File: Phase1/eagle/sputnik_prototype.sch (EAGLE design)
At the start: 83 parts, among them U1 MEGA128-M, U2 MIC5219 3.3V, Y1 32MHz, Y2 8MHZ

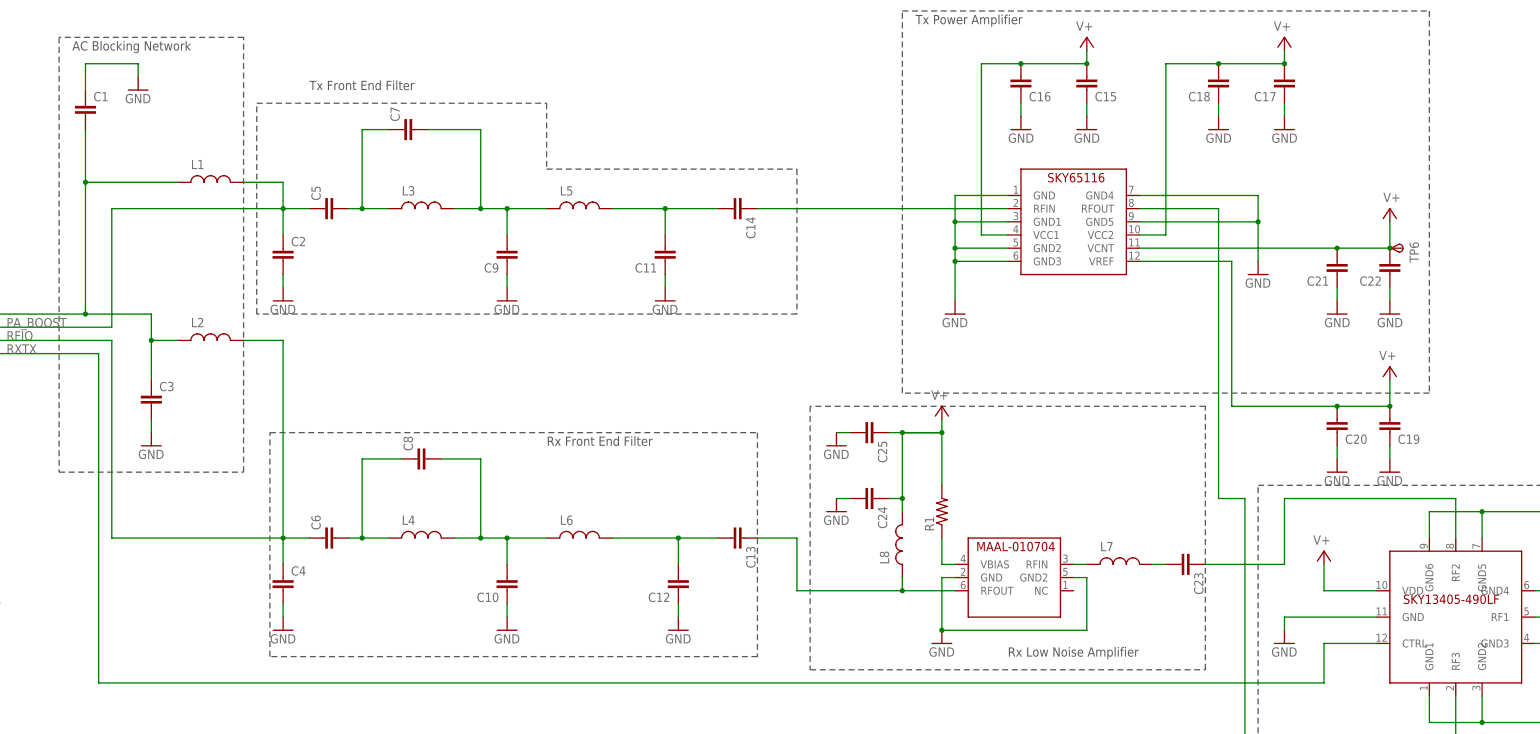
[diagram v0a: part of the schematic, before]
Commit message: Updated RF schematic
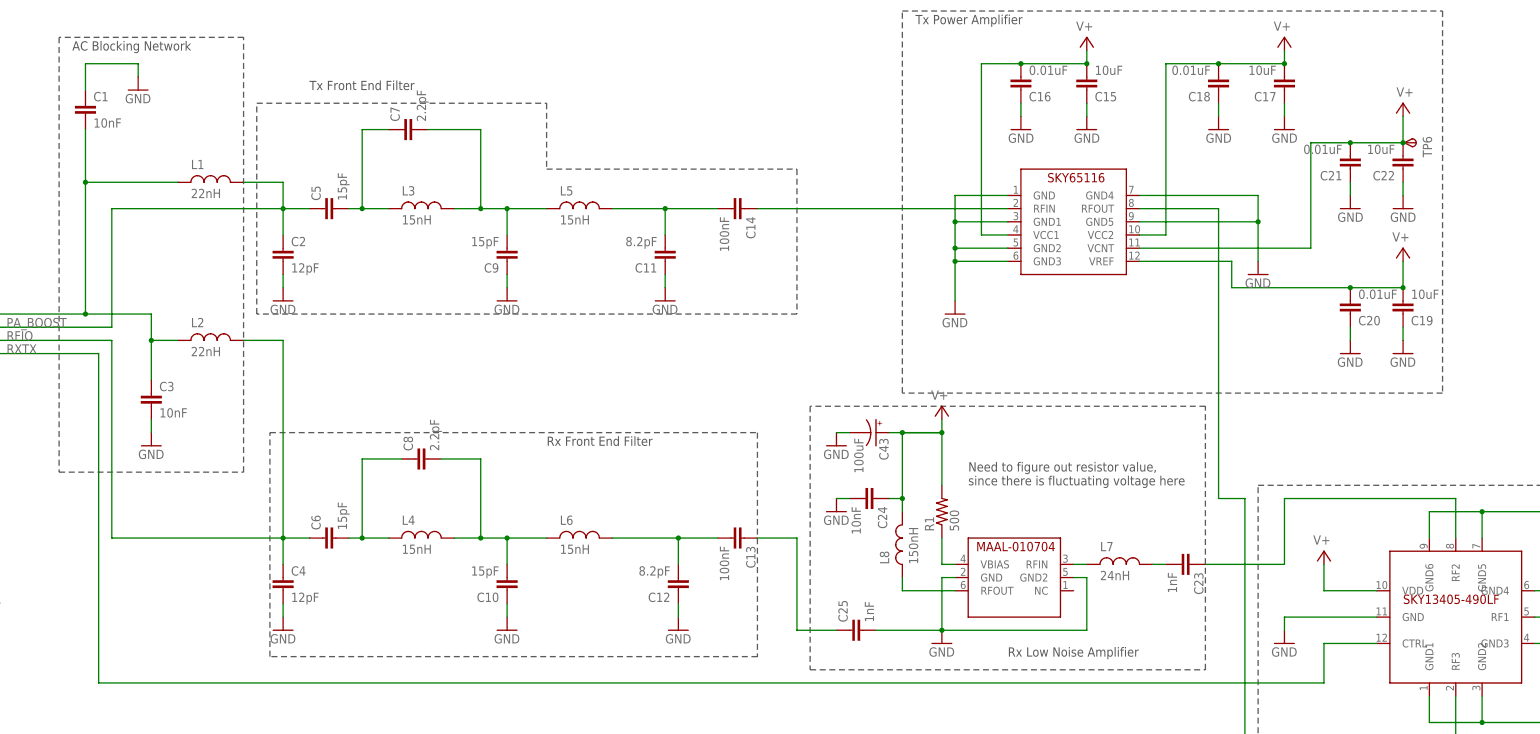
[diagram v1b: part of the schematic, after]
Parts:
- added C43: 100uF, rcl:CPOL-USCT6032
- C1, C3: value (none) -> 10nF
- C10, C5, C6, C9: value (none) -> 15pF
- C11, C12: value (none) -> 8.2pF
- C13, C14: value (none) -> 100nF
- C15, C17, C19, C22: value (none) -> 10uF
- C16, C18, C20, C21: value (none) -> 0.01uF
- C2, C4: value (none) -> 12pF
- C23, C25: value (none) -> 1nF; device rcl_custom:C-EU0603-B-NOSILK -> rcl_custom:C-EU0402-B-NOSILK
- C24: value (none) -> 10nF; device rcl_custom:C-EU0603-B-NOSILK -> rcl_custom:C-EU0402-B-NOSILK
- C7, C8: value (none) -> 2.2pF
- L1, L2: value (none) -> 22nH
- L3, L4, L5, L6: value (none) -> 15nH
- L7: value (none) -> 24nH; device rcl_custom:L-US0603-B-NOSILK -> rcl_custom:L-US0402-B-NOSILK
- L8: value (none) -> 150nH
- R1: value (none) -> 500
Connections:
- new net N$7: L8.1, U$4.RFOUT
- net GND: now also C43.-
- net N$4: now also C25.1; no longer L8.1, U$4.RFOUT
- net V+: now also C43.+; no longer C25.1
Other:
- note added: "Need to figure out resistor value, since there is fluctuating voltage here"
- moved on the sheet: C19, C20, C21, C22, C25, TP6

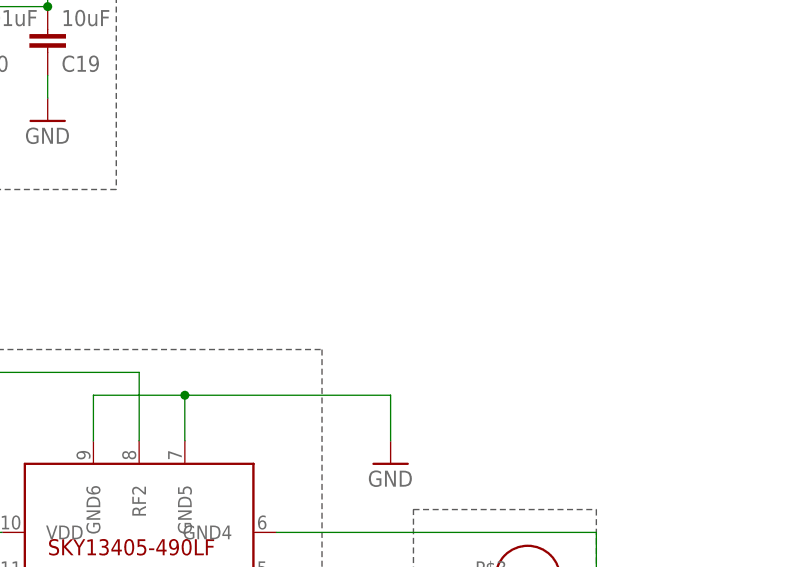
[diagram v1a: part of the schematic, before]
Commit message: Updated RF schematic
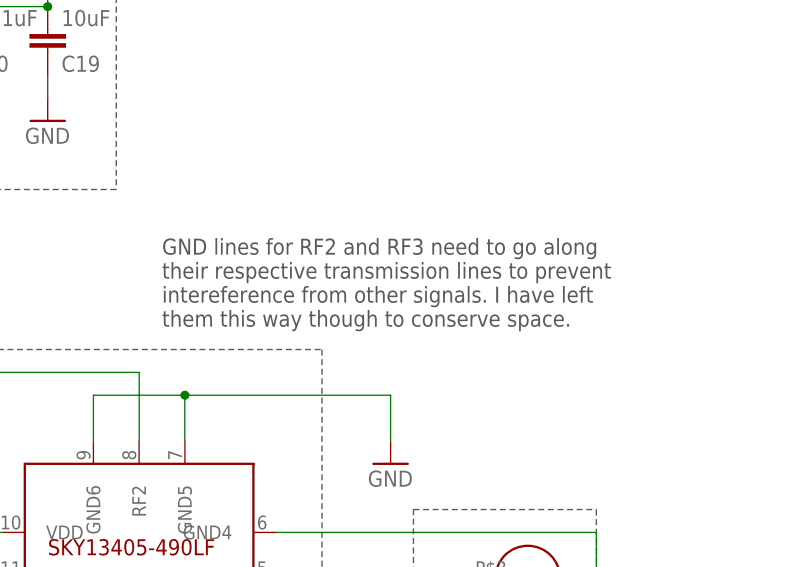
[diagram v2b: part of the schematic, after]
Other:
- note added: "GND lines for RF2 and RF3 need to go along their respective transmission lines to prevent intereference from other signals. I have left them this way though to conserve space."
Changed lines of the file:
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@@
 <?xml version="1.0" encoding="utf-8"?>
 <!DOCTYPE eagle SYSTEM "eagle.dtd">
-<eagle version="7.5.0">
+<eagle version="7.4.0">
 <drawing>
 <settings>
@@
 <text x="406.4" y="332.74" size="1.778" layer="97">Need to figure out resistor value,
 since there is fluctuating voltage here</text>
+<text x="502.92" y="335.28" size="1.778" layer="97">GND lines for RF2 and RF3 need to go along
+their respective transmission lines to prevent
+intereference from other signals. I have left
+them this way though to conserve space.</text>
 </plain>
 <instances>

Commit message: Updated the schematic a bit. Removed I2C line to payload and sense pin
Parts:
- removed JP6: (no value), psas_c3_team05:PINHD-1X2
- removed JP7: (no value), pinhead:PINHD-1X3
- removed TP2, TP3, TP6, TP7, TP8, TP9: TPSPAD1-13, testpad:TPSPAD1-13
- C23: value 1nF -> (none)
- C24: value 10nF -> (none)
- C43: value 100uF -> (none)
- L7: value 24nH -> (none)
- L8: value 150nH -> (none)
- R1: value 500 -> (none)
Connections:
- net PE4: no longer JP7.1, TP7.PP
- net PE5: no longer JP7.2, TP8.PP
- net PE6: no longer JP7.3, TP9.PP
- net SDA: no longer JP6.2, TP3.PP
- net SDL: no longer JP6.1, TP2.PP
- net V+: no longer TP6.PP
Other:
- note added: "Need to figure out values for LNA"
- note removed: "Need to figure out resistor value, since there is fluctuating voltage here"
- note removed: "Sense"
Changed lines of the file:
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@@
 <part name="U$4" library="sputnik" deviceset="MAAL-010704" device=""/>
 <part name="GND24" library="psas_c3_team05" deviceset="GND" device=""/>
-<part name="R1" library="rcl_custom" deviceset="R-US_" device="0603-B-NOSILK" value="500"/>
-<part name="L8" library="rcl_custom" deviceset="L-US" device="0603-B-NOSILK" value="150nH"/>
+<part name="R1" library="rcl_custom" deviceset="R-US_" device="0603-B-NOSILK"/>
+<part name="L8" library="rcl_custom" deviceset="L-US" device="0603-B-NOSILK"/>
 <part name="GND26" library="psas_c3_team05" deviceset="GND" device=""/>
 <part name="SUPPLY10" library="psas_c3_team05" deviceset="V+" device=""/>
@@
 <part name="U$6" library="psas_c3_team05" deviceset="SKY65116" device=""/>
 <part name="JP5" library="psas_c3_team05" deviceset="PINHD-1X2" device=""/>
-<part name="JP6" library="psas_c3_team05" deviceset="PINHD-1X2" device=""/>
-<part name="JP7" library="pinhead" deviceset="PINHD-1X3" device=""/>
 <part name="U2" library="Lilypad_Arduino_USB_v12" deviceset="SPARKFUN-POWERIC_V_REG_MIC5219" device="3.3V" value="MIC5219 3.3V"/>
 <part name="SUPPLY12" library="psas_c3_team05" deviceset="V+" device=""/>
@@
 <part name="P+4" library="SparkFun-v5" deviceset="3.3V" device=""/>
 <part name="TP1" library="testpad" deviceset="TPS" device="PAD1-13"/>
-<part name="TP2" library="testpad" deviceset="TPS" device="PAD1-13"/>
-<part name="TP3" library="testpad" deviceset="TPS" device="PAD1-13"/>
 <part name="TP4" library="testpad" deviceset="TPS" device="PAD1-13"/>
 <part name="TP5" library="testpad" deviceset="TPS" device="PAD1-13"/>
-<part name="TP7" library="testpad" deviceset="TPS" device="PAD1-13"/>
-<part name="TP8" library="testpad" deviceset="TPS" device="PAD1-13"/>
-<part name="TP9" library="testpad" deviceset="TPS" device="PAD1-13"/>
 <part name="TP10" library="testpad" deviceset="TPS" device="PAD1-13"/>
 <part name="TP11" library="testpad" deviceset="TPS" device="PAD1-13"/>
@@
 <part name="C42" library="rcl_custom" deviceset="C-EU" device="0603-B-NOSILK" value="470pF"/>
 <part name="GND36" library="psas_c3_team05" deviceset="GND" device=""/>
-<part name="TP6" library="testpad" deviceset="TPS" device="PAD1-13"/>
-<part name="C23" library="rcl_custom" deviceset="C-EU" device="0402-B-NOSILK" value="1nF"/>
-<part name="C24" library="rcl_custom" deviceset="C-EU" device="0402-B-NOSILK" value="10nF"/>
+<part name="C23" library="rcl_custom" deviceset="C-EU" device="0402-B-NOSILK"/>
+<part name="C24" library="rcl_custom" deviceset="C-EU" device="0402-B-NOSILK"/>
 <part name="C25" library="rcl_custom" deviceset="C-EU" device="0402-B-NOSILK" value="1nF"/>
-<part name="C43" library="rcl" deviceset="CPOL-US" device="CT6032" value="100uF"/>
-<part name="L7" library="rcl_custom" deviceset="L-US" device="0402-B-NOSILK" value="24nH"/>
+<part name="C43" library="rcl" deviceset="CPOL-US" device="CT6032"/>
+<part name="L7" library="rcl_custom" deviceset="L-US" device="0402-B-NOSILK"/>
 </parts>
 <sheets>
@@
 <text x="12.7" y="345.44" size="1.778" layer="97">Payload interface</text>
 <text x="15.24" y="335.28" size="1.778" layer="97">UART</text>
-<text x="17.78" y="317.5" size="1.778" layer="97">i2c</text>
-<text x="15.24" y="299.72" size="1.778" layer="97">Sense</text>
-<text x="406.4" y="332.74" size="1.778" layer="97">Need to figure out resistor value,
-since there is fluctuating voltage here</text>
+<text x="406.4" y="332.74" size="1.778" layer="97">Need to figure out values for LNA</text>
 <text x="502.92" y="335.28" size="1.778" layer="97">GND lines for RF2 and RF3 need to go along
 their respective transmission lines to prevent
@@
 <instance part="U$6" gate="G$1" x="426.72" y="383.54"/>
 <instance part="JP5" gate="G$1" x="25.4" y="335.28" rot="MR0"/>
-<instance part="JP6" gate="G$1" x="25.4" y="317.5" rot="MR0"/>
-<instance part="JP7" gate="A" x="25.4" y="299.72" rot="MR0"/>
 <instance part="U2" gate="G$1" x="96.52" y="20.32"/>
 <instance part="SUPPLY12" gate="1" x="63.5" y="33.02"/>
@@
 <instance part="P+4" gate="G$1" x="215.9" y="304.8"/>
 <instance part="TP1" gate="G$1" x="119.38" y="33.02"/>
-<instance part="TP2" gate="G$1" x="50.8" y="322.58"/>
-<instance part="TP3" gate="G$1" x="48.26" y="320.04"/>
 <instance part="TP4" gate="G$1" x="50.8" y="340.36"/>
 <instance part="TP5" gate="G$1" x="48.26" y="337.82"/>
-<instance part="TP7" gate="G$1" x="45.72" y="304.8"/>
-<instance part="TP8" gate="G$1" x="43.18" y="302.26"/>
-<instance part="TP9" gate="G$1" x="40.64" y="299.72"/>
 <instance part="TP10" gate="G$1" x="55.88" y="203.2"/>
 <instance part="TP11" gate="G$1" x="53.34" y="200.66"/>
@@
 </instance>
 <instance part="GND36" gate="1" x="111.76" y="5.08"/>
-<instance part="TP6" gate="G$1" x="492.76" y="398.78" rot="R270"/>
 <instance part="C23" gate="CE" x="449.58" y="317.5" rot="R270"/>
 <instance part="C24" gate="CE" x="388.62" y="330.2" rot="R270"/>
@@
 <pinref part="C22" gate="CE" pin="2"/>
 <junction x="490.22" y="398.78"/>
-<pinref part="TP6" gate="G$1" pin="PP"/>
 <wire x1="490.22" y1="398.78" x2="490.22" y2="403.86" width="0.1524" layer="91"/>
 <pinref part="U$6" gate="G$1" pin="VCNT"/>
@@
 <segment>
 <pinref part="JP2" gate="G$1" pin="1"/>
-<wire x1="30.48" y1="220.98" x2="53.34" y2="220.98" width="0.1524" layer="91"/>
-<wire x1="53.34" y1="220.98" x2="228.6" y2="220.98" width="0.1524" layer="91"/>
+<wire x1="30.48" y1="220.98" x2="228.6" y2="220.98" width="0.1524" layer="91"/>
 <wire x1="228.6" y1="220.98" x2="228.6" y2="78.74" width="0.1524" layer="91"/>
 <pinref part="U1" gate="G$1" pin="(SCL/INT0)PD0"/>
 <wire x1="228.6" y1="78.74" x2="198.12" y2="78.74" width="0.1524" layer="91"/>
 <label x="38.1" y="220.98" size="1.778" layer="95"/>
-<pinref part="JP6" gate="G$1" pin="1"/>
-<wire x1="27.94" y1="320.04" x2="50.8" y2="320.04" width="0.1524" layer="91"/>
-<wire x1="50.8" y1="320.04" x2="53.34" y2="320.04" width="0.1524" layer="91"/>
-<wire x1="53.34" y1="320.04" x2="53.34" y2="220.98" width="0.1524" layer="91"/>
-<junction x="53.34" y="220.98"/>
-<label x="33.02" y="320.04" size="1.778" layer="95"/>
-<pinref part="TP2" gate="G$1" pin="PP"/>
-<junction x="50.8" y="320.04"/>
 </segment>
 </net>
@@
 <segment>
 <pinref part="JP2" gate="G$1" pin="2"/>
-<wire x1="30.48" y1="218.44" x2="50.8" y2="218.44" width="0.1524" layer="91"/>
-<wire x1="50.8" y1="218.44" x2="226.06" y2="218.44" width="0.1524" layer="91"/>
+<wire x1="30.48" y1="218.44" x2="226.06" y2="218.44" width="0.1524" layer="91"/>
 <wire x1="226.06" y1="218.44" x2="226.06" y2="81.28" width="0.1524" layer="91"/>
 <pinref part="U1" gate="G$1" pin="(SDA/INT1)PD1"/>
 <wire x1="226.06" y1="81.28" x2="198.12" y2="81.28" width="0.1524" layer="91"/>
 <label x="38.1" y="218.44" size="1.778" layer="95"/>
-<pinref part="JP6" gate="G$1" pin="2"/>
-<wire x1="27.94" y1="317.5" x2="48.26" y2="317.5" width="0.1524" layer="91"/>
-<wire x1="48.26" y1="317.5" x2="50.8" y2="317.5" width="0.1524" layer="91"/>
-<wire x1="50.8" y1="317.5" x2="50.8" y2="218.44" width="0.1524" layer="91"/>
-<junction x="50.8" y="218.44"/>
-<label x="33.02" y="317.5" size="1.778" layer="95"/>
-<pinref part="TP3" gate="G$1" pin="PP"/>
-<junction x="48.26" y="317.5"/>
 </segment>
 </net>
@@
 <segment>
 <pinref part="U1" gate="G$1" pin="(OC3B/INT4)PE4"/>
-<pinref part="JP7" gate="A" pin="1"/>
-<wire x1="27.94" y1="302.26" x2="45.72" y2="302.26" width="0.1524" layer="91"/>
-<wire x1="45.72" y1="302.26" x2="96.52" y2="302.26" width="0.1524" layer="91"/>
 <wire x1="96.52" y1="302.26" x2="96.52" y2="228.6" width="0.1524" layer="91"/>
 <wire x1="96.52" y1="228.6" x2="254" y2="228.6" width="0.1524" layer="91"/>
 <wire x1="254" y1="228.6" x2="254" y2="66.04" width="0.1524" layer="91"/>
 <wire x1="254" y1="66.04" x2="198.12" y2="66.04" width="0.1524" layer="91"/>
-<label x="33.02" y="302.26" size="1.778" layer="95"/>
-<pinref part="TP7" gate="G$1" pin="PP"/>
-<junction x="45.72" y="302.26"/>
 </segment>
 </net>
@@
 <segment>
 <pinref part="U1" gate="G$1" pin="(OC3C/INT5)PE5"/>
-<pinref part="JP7" gate="A" pin="2"/>
-<wire x1="27.94" y1="299.72" x2="43.18" y2="299.72" width="0.1524" layer="91"/>
-<wire x1="43.18" y1="299.72" x2="93.98" y2="299.72" width="0.1524" layer="91"/>
 <wire x1="93.98" y1="299.72" x2="93.98" y2="226.06" width="0.1524" layer="91"/>
 <wire x1="93.98" y1="226.06" x2="251.46" y2="226.06" width="0.1524" layer="91"/>
 <wire x1="251.46" y1="226.06" x2="251.46" y2="68.58" width="0.1524" layer="91"/>
 <wire x1="251.46" y1="68.58" x2="198.12" y2="68.58" width="0.1524" layer="91"/>
-<label x="33.02" y="299.72" size="1.778" layer="95"/>
-<pinref part="TP8" gate="G$1" pin="PP"/>
-<junction x="43.18" y="299.72"/>
 </segment>
 </net>
@@
 <segment>
 <pinref part="U1" gate="G$1" pin="(T3/INT6)PE6"/>
-<pinref part="JP7" gate="A" pin="3"/>
-<wire x1="27.94" y1="297.18" x2="40.64" y2="297.18" width="0.1524" layer="91"/>
-<wire x1="40.64" y1="297.18" x2="91.44" y2="297.18" width="0.1524" layer="91"/>
 <wire x1="91.44" y1="297.18" x2="91.44" y2="223.52" width="0.1524" layer="91"/>
 <wire x1="91.44" y1="223.52" x2="248.92" y2="223.52" width="0.1524" layer="91"/>
 <wire x1="248.92" y1="223.52" x2="248.92" y2="71.12" width="0.1524" layer="91"/>
 <wire x1="248.92" y1="71.12" x2="198.12" y2="71.12" width="0.1524" layer="91"/>
-<label x="33.02" y="297.18" size="1.778" layer="95"/>
-<pinref part="TP9" gate="G$1" pin="PP"/>
-<junction x="40.64" y="297.18"/>
-</segment>
-</net>
+</segment>
+</net>

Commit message: Updated schematic, added LDO datasheet
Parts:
- added C44, C45: 10uF, rcl_custom:C-EU0603-B-NOSILK
- added U$3: LD39200, psas_c3_team05:LD39200
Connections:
- new net N$26: C24.1, C43.+, L8.2, R1.2
- net GND: now also C44.1, C45.1, U$3.GND
- net V+: now also C44.2, C45.2, U$3.ADJ, U$3.EN, U$3.IN, U$3.OUT; no longer C24.1, C43.+, L8.2, R1.2

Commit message: Fixed some stuff on schematic
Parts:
- removed C13: 100nF, rcl_custom:C-EU0603-B-NOSILK
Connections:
- removed net N$4: C13.1, C25.1
- removed net PE4: U1.(OC3B/INT4)PE4
- removed net PE5: U1.(OC3C/INT5)PE5
- removed net PE6: U1.(T3/INT6)PE6
- net GND: no longer C25.2
- net N$20: now also C25.1; no longer C13.2
- net N$7: now also C25.2
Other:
- note added: "Need different LDO supply"
- moved on the sheet: C1
